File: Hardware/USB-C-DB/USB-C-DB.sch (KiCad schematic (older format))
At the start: 64 parts, among them J1 USB_C_Receptacle, J2 BatTP+, J3 JST Battery con, J4 BatTP-, U1 FT260S-U

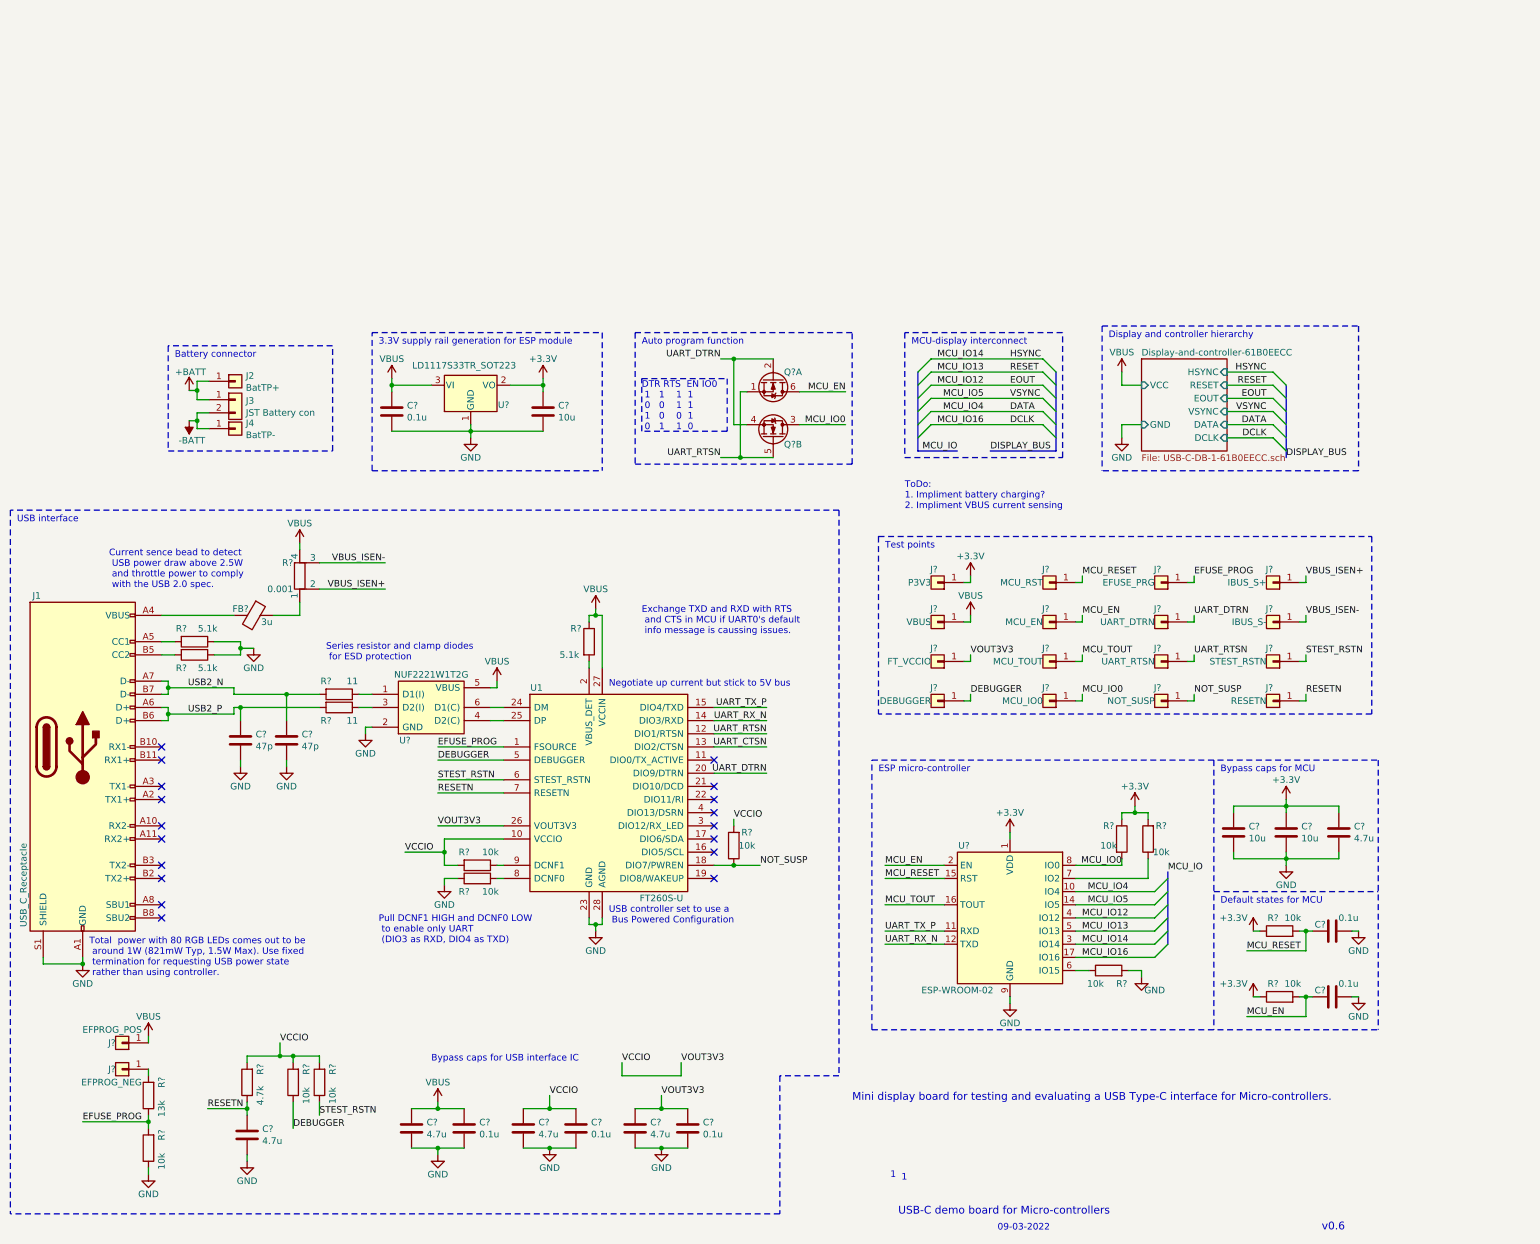
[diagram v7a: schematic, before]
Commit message: Finalizing schematic for BOM analysis
* Replacing MOSFET parts with higher current version.
* Re-adding 555 based brightness control circuit.
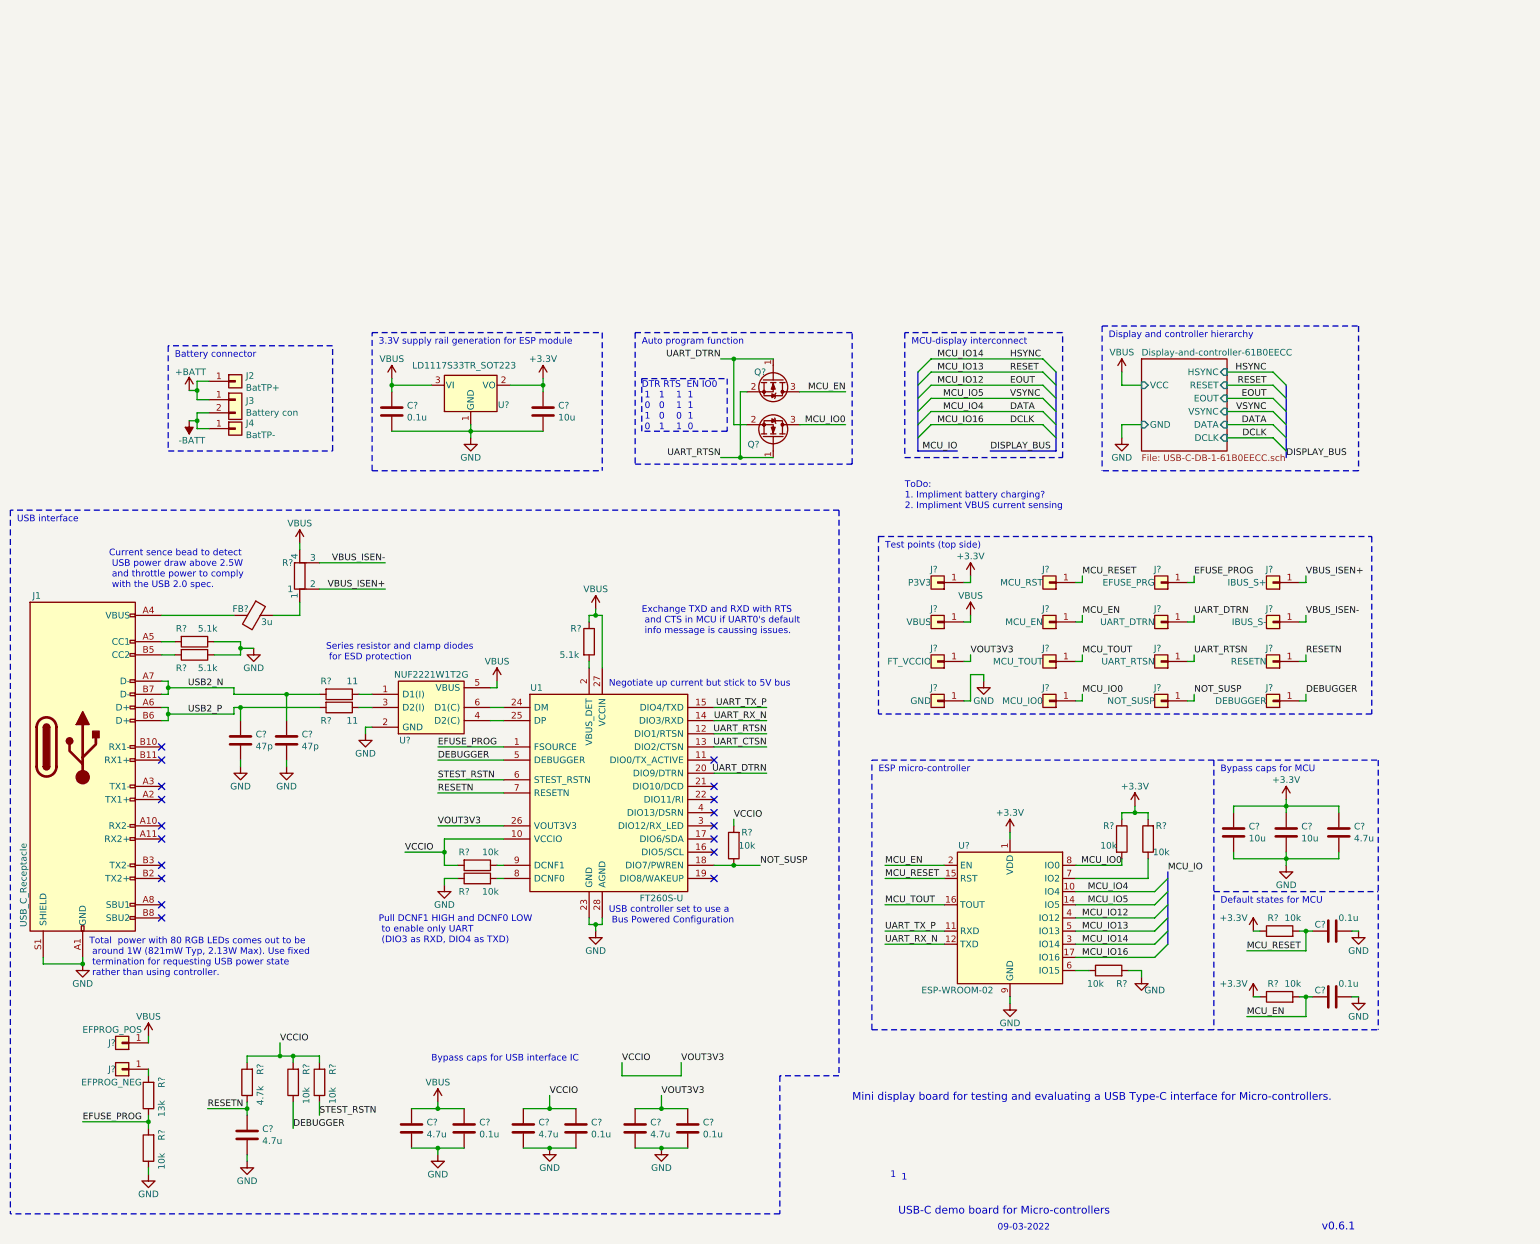
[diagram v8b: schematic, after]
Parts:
- removed Q? (x2): 2N7002KDW_R1_00001_seperate, SOT65P210X110-6N, symbol USB-C-DB-rescue:2N7002KDW_R1_00001_seperate
- added Q? (x2): XP262N7002TR-G, Package_TO_SOT_SMD:SOT-23, symbol USB-C-DB-rescue:XP262N7002TR-G
- J3: value JST Battery con -> Battery con
- J?: value DEBUGGER -> GND
- J?: value STEST_RSTN -> RESETN
- J?: value RESETN -> DEBUGGER
- R?: value 0.001 -> 1; footprint Resistor_SMD:R_0201_0603Metric_Pad0.64x0.40mm_HandSolder -> Resistor_SMD:R_0603_1608Metric_Pad0.98x0.95mm_HandSolder; MPN RC0201DR-071ML -> RT0603DRE071RL
- U?: MPN (none) -> ESP-WROOM-02D-N2
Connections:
- net DEBUGGER: now also J?.1 (Pin_1); no longer J?.1 (Pin_1)
- net GND: now also J?.1 (Pin_1)
- net MCU_EN: now also Q?.3 (D)
- net MCU_IO0: now also Q?.3 (D)
- net RESETN: now also J?.1 (Pin_1); no longer J?.1 (Pin_1)
- net STEST_RSTN: no longer J?.1 (Pin_1)
- net UART_DTRN: now also Q?.1 (G), Q?.2 (S)
- net UART_RTSN: now also Q?.1 (G), Q?.2 (S)
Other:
- note added: "Test points (top side)"
- note added: "Total power with 80 RGB LEDs comes out to be\n around 1W (821mW Typ, 2.13W Max). Use fixed\n termination for requesting USB power state\n rather than using controller."
- note added: "v0.6.1"
- note removed: "Test points"
- note removed: "Total power with 80 RGB LEDs comes out to be\n around 1W (821mW Typ, 1.5W Max). Use fixed\n termination for requesting USB power state\n rather than using controller."
- note removed: "v0.6"
